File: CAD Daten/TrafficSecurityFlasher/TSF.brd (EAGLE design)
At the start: 160 x 100 mm, 5 parts, among them IC1 TINY15LS

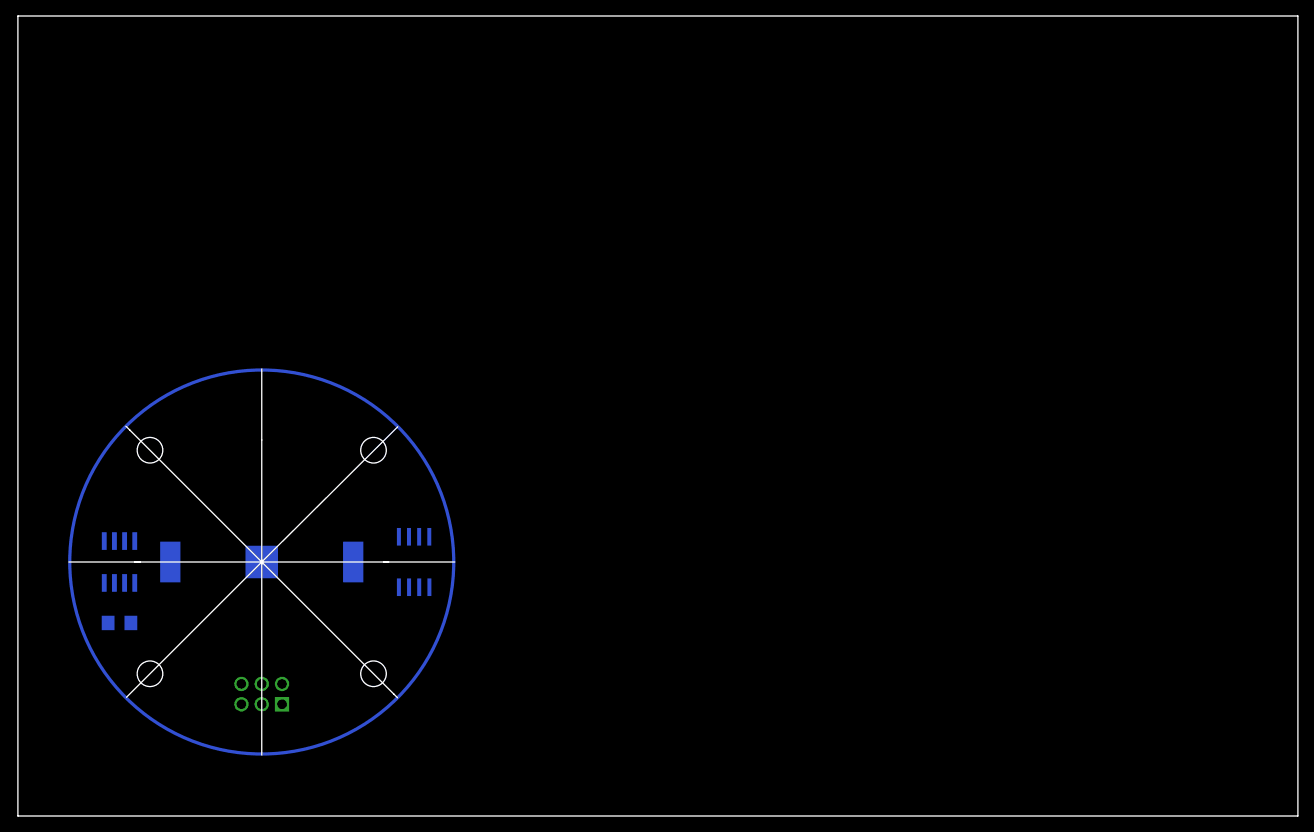
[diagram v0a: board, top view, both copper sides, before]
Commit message: 
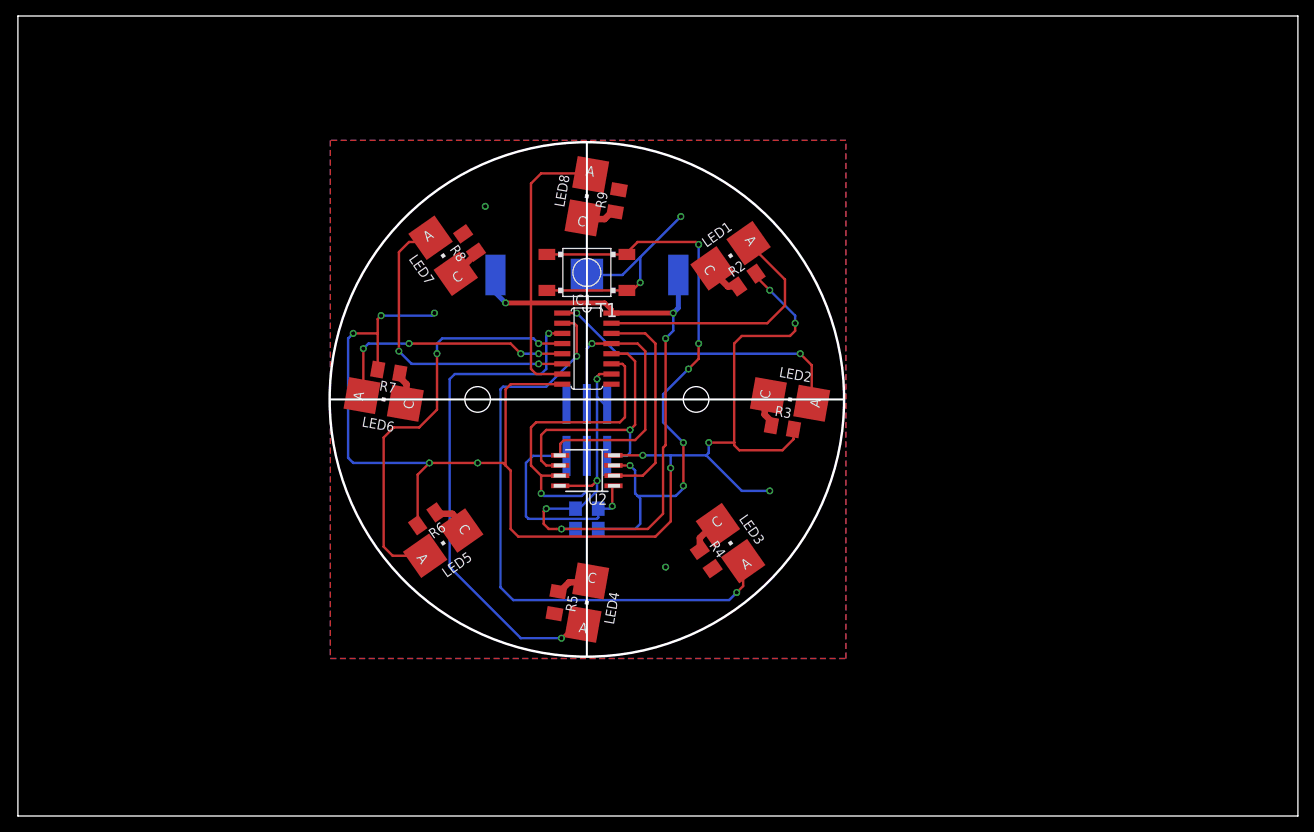
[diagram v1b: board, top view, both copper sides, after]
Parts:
- removed U$1: TINY138S2, Atmel - µController:SO08
- added LED1, LED2, LED3, LED4, LED5, LED6, LED7, LED8: (no value), led:P-LCC-2
- added R10: 10k, rcl:R1206
- added R2, R3, R4, R5, R6, R7, R8, R9: (no value), rcl:M1206
- added T1: OMRON-B3S-1002P, Taster - Omron B3S-1002P:B3S-1002P
- added U2: ATTINY85-S, _hhn_attiny25_45_85:SOIC8_EIAJ_208MIL
- IC1: value TINY15LS -> (none); device atmel:SOIC8 -> 74_er Reihe (DIN Europa):SO16
- XW1: device Atmel - ISP_6 (AVR ISP MKII):WSL -> Atmel - ISP_6 (AVR ISP MKII):WSL_SMD
- moved R1 60.1 mm to (71.1, 38.4)
- moved U1 54.2 mm to (71.1, 67.6)
- moved XW1 52.4 mm to (71.1, 48.3)
- moved IC1 34.3 mm to (71.1, 58.4), flipped to the top, turned to 270 degrees
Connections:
- removed net +3V2: IC1.8, R1.1, U$1.8, U1.+$1, U1.+$2, XW1.2
- new net DATA0: IC1.15, LED1.A
- new net DATA1: IC1.1, LED2.A
- new net DATA2: IC1.2, LED3.A
- new net DATA3: IC1.3, LED4.A
- new net DATA4: IC1.4, LED5.A
- new net DATA5: IC1.5, LED6.A
- new net DATA6: IC1.6, LED7.A
- new net DATA7: IC1.7, LED8.A
- new net GND: XW1.6
- new net N$10: LED5.C, R6.1
- new net N$11: LED6.C, R7.1
- new net N$12: LED7.C, R8.1
- new net N$13: LED8.C, R9.1
- new net N$6: LED1.C, R2.1
- new net N$7: LED2.C, R3.1
- new net N$8: LED3.C, R4.1
- new net N$9: LED4.C, R5.1
- new net VCC: IC1.10, IC1.16, R1.1, R10.1, U1.+$1, U1.+$2, U2.8, XW1.2
- net AGND: now also IC1.8, R2.2, R3.2, R4.2, R5.2, R6.2, R7.2, R8.2, R9.2, T1.3, T1.4, U2.4; no longer IC1.4, U$1.4, XW1.6
- net PORTB.0: now also IC1.13, U2.5; no longer U$1.5
- net PORTB.1: now also IC1.12, U2.6; no longer U$1.6
- net PORTB.2: now also IC1.11, U2.7; no longer U$1.7
- net PORTB.3: now also IC1.14, U2.2; no longer U$1.2
- net PORTB.4: now also R10.2, T1.1, T1.2, U2.3; no longer U$1.3
- net PORTB.5: now also U2.1; no longer U$1.1
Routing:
- net AGND: track 0.00 -> 211.5 mm, vias 0 -> 15
- net VCC: track 0.00 -> 106.1 mm, vias 0 -> 7
- net DATA2: track 0.00 -> 76.6 mm, vias 0 -> 2
- net PORTB.4: track 0.00 -> 74.5 mm, vias 0 -> 6
- net DATA3: track 0.00 -> 63.4 mm, vias 0 -> 2
- net DATA4: track 0.00 -> 51.9 mm, vias 0 -> 2
- net PORTB.2: track 0.00 -> 42.1 mm, vias 0 -> 1
- net DATA1: track 0.00 -> 39.7 mm, vias 0 -> 2
- net DATA6: track 0.00 -> 38.2 mm, vias 0 -> 2
- net PORTB.0: track 0.00 -> 37.5 mm, vias 0 -> 1
- net DATA7: track 0.00 -> 35.4 mm
- net PORTB.1: track 0.00 -> 35.3 mm, vias 0 -> 1
- net DATA0: track 0.00 -> 34.1 mm
- net DATA5: track 0.00 -> 31.6 mm, vias 0 -> 4
- net PORTB.5: track 0.00 -> 27.0 mm, vias 0 -> 1
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- added copper zone on layer 1, net AGND
- added copper zone on layer 16, net AGND
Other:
- outline, holes or cut-outs redrawn

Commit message: 
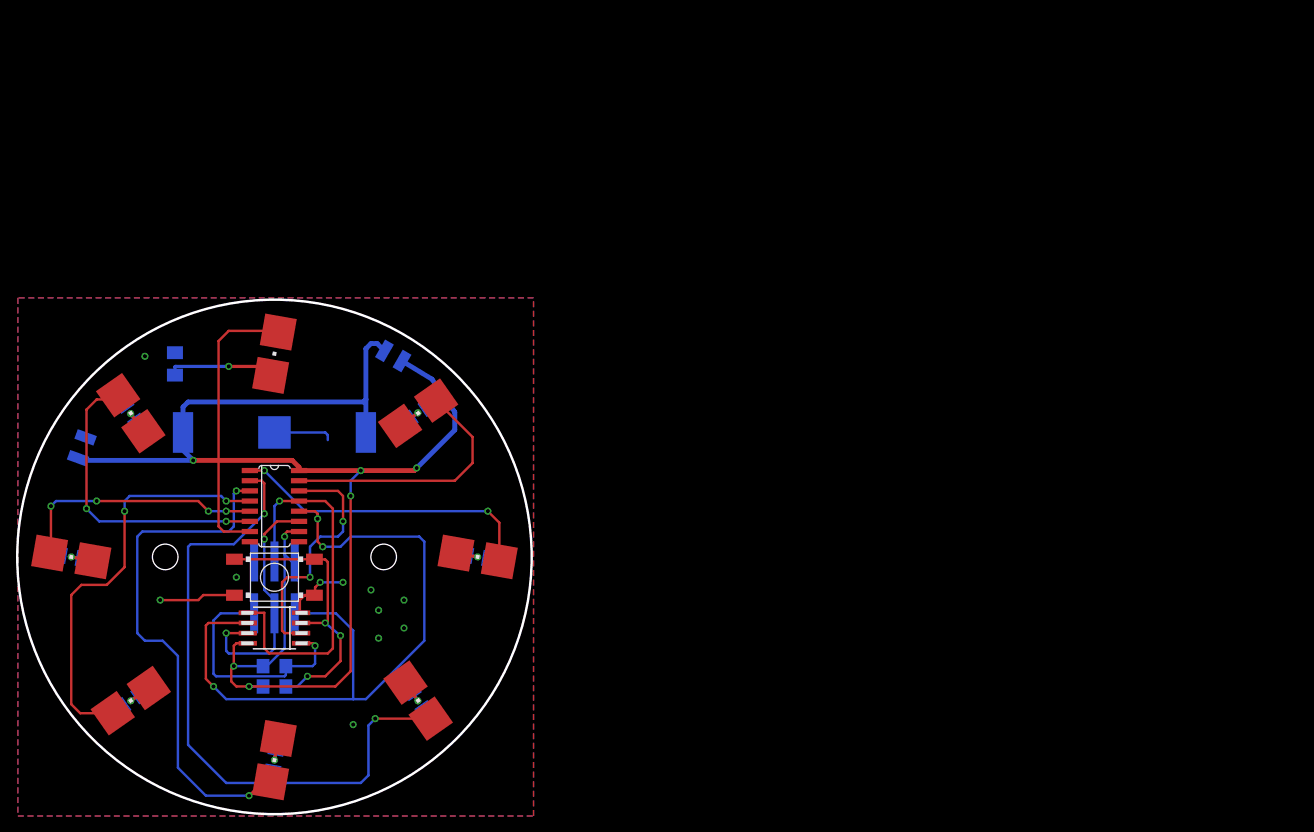
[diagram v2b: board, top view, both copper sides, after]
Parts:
- added PAD1, PAD2: (no value), wirepad:SMD1,27-2,54
- added SJ1: (no value), jumper:SJW
- added U$1: (no value), !!!Platinen_Logo!!!:25X25_BEST
- moved R9 58.9 mm to (19.6, 56.5), flipped to the bottom, turned to 90 degrees
- moved T1 54.6 mm to (32.1, 29.8)
- moved R8 47.4 mm to (14.1, 50.3), flipped to the bottom, turned to 55 degrees
- moved R7 46.0 mm to (6.67, 32.4), flipped to the bottom, turned to 10 degrees
- moved R2 44.3 mm to (50.0, 50.3), flipped to the bottom, turned to 145 degrees
- moved IC1 43.7 mm to (32.1, 38.7)
- moved LED4 43.7 mm to (32.1, 6.99)
- moved LED8 43.7 mm to (32.1, 57.8)
- moved R1 43.7 mm to (32.1, 18.7)
- moved R10 43.7 mm to (32.1, 16.2)
- moved U1 43.7 mm to (32.1, 47.9)
- moved U2 43.7 mm to (32.1, 23.5)
- moved XW1 43.7 mm to (32.1, 28.6)
- moved LED1 43.7 mm to (50.0, 50.3)
- moved LED2 43.7 mm to (57.5, 32.4)
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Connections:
- new net N$1: SJ1.1, U1.+$1, U1.+$2
- net AGND: now also PAD2.1
- net VCC: now also PAD1.1, SJ1.2; no longer U1.+$1, U1.+$2
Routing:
- net AGND: track 211.5 -> 26.7 mm, vias 15 -> 11
- net PORTB.1: track 35.3 -> 92.9 mm, vias 1 -> 3
- net N$1: track 0.00 -> 39.9 mm
- net PORTB.4: track 74.5 -> 36.4 mm, vias 6 -> 3
- net VCC: track 106.1 -> 138.3 mm
- net PORTB.2: track 42.1 -> 31.2 mm, vias 1 -> 2
- net PORTB.0: track 37.5 -> 47.9 mm
- net N$13: track 4.43 -> 13.7 mm, vias 0 -> 1
- net DATA2: track 76.6 -> 81.0 mm
- net PORTB.3: track 26.8 -> 31.2 mm, vias 0 -> 2
- net PORTB.5: track 27.0 -> 30.6 mm
- net N$9: track 4.60 -> 7.09 mm, vias 0 -> 1
- net DATA3: track 63.4 -> 64.9 mm
- net N$6: track 4.29 -> 5.64 mm, vias 0 -> 1
- net N$8: track 4.47 -> 5.74 mm, vias 0 -> 1
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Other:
- board size 160 x 100 mm -> 64.3 x 64.3 mm
- board text added: "Modus"
